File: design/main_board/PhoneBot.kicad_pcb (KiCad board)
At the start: 2 copper layers, 41.3 x 103 mm, 88 parts, among them J101 CX70M-24P1, J102 AVR-ISP-6, J103 Conn_02x03_Odd_Even, J104 Conn_02x03_Odd_Even, J105 Conn_02x03_Odd_Even, J106 Conn_02x03_Odd_Even, SW301 SW_SPDT, U101 ATmega32U4-AU, U201 RN4871, U301 AP2138N-3.3TRG1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

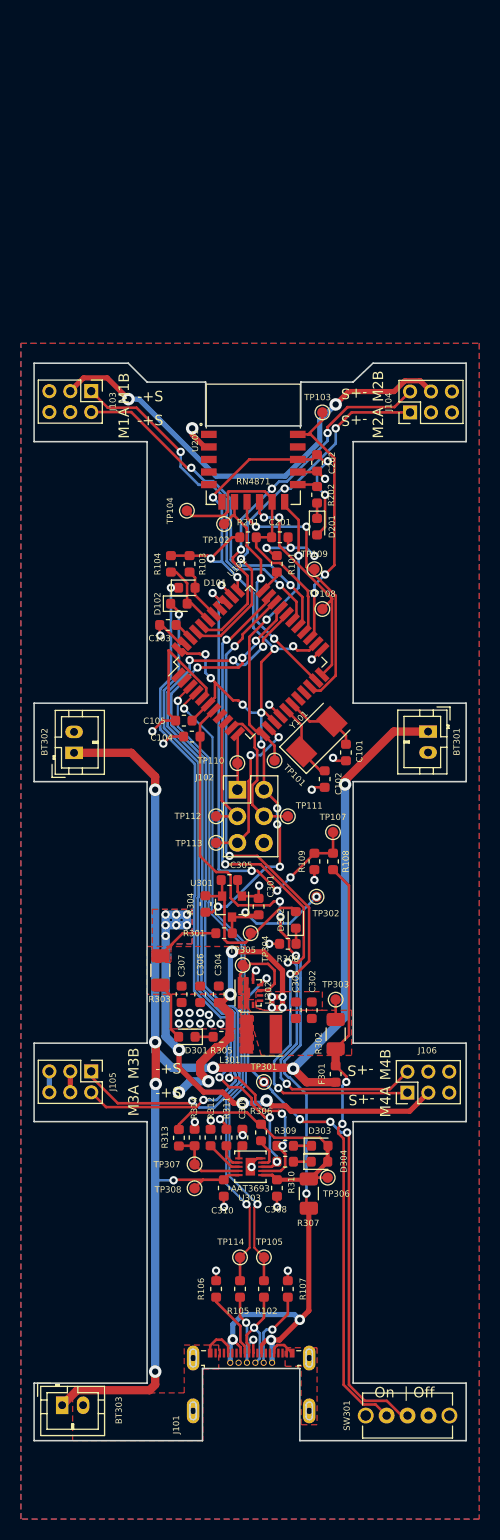
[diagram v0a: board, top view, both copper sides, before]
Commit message: Created esp32 footprint and symbol
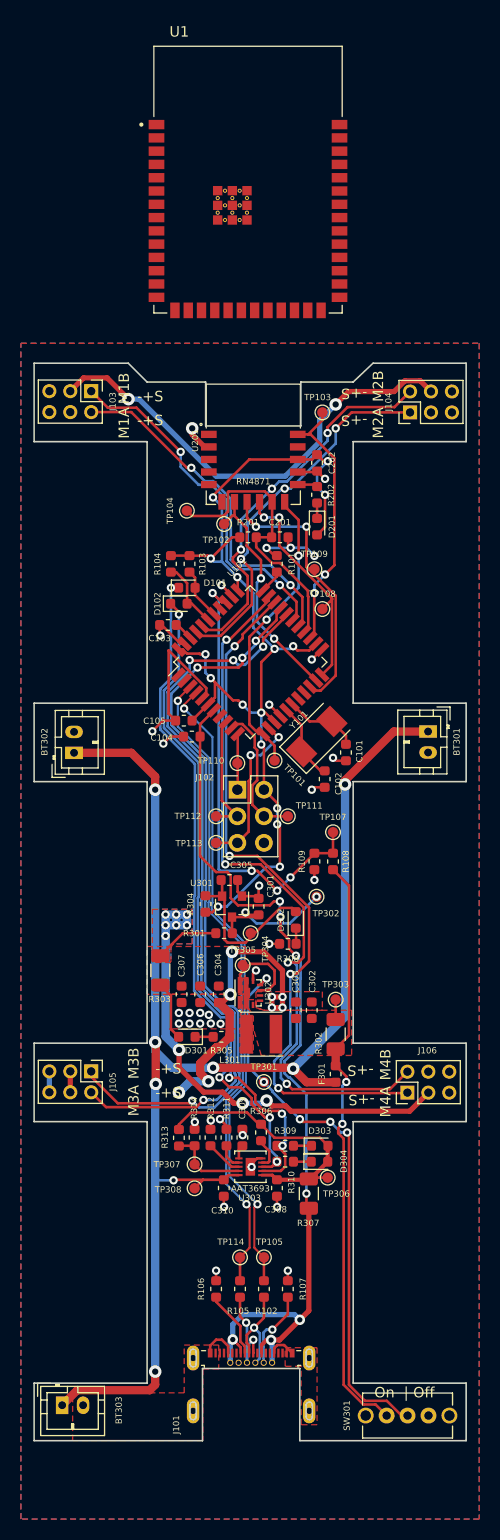
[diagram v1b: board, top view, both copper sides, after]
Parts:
- added U1: ESP32-S3-WROOM-1-N16R8, CustomFootprints:XCVR_ESP32-S3-WROOM-1-N16R8, F.Cu at (-0.25, -53.8)
- R108: value 1k -> 1M
- R109: value 3.6k -> 3.6M
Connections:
- net /VBAT_SENSE renamed /PowerSheet/Vbat
- net /~BLE_RST renamed /~{BLE_RST}
- net /~RST renamed /~{RST}
- J101 pad A10: (no net) -> unconnected-(J101-PadA10)
- J101 pad A11: (no net) -> unconnected-(J101-PadA11)
- J101 pad A2: (no net) -> unconnected-(J101-PadA2)
- J101 pad A3: (no net) -> unconnected-(J101-PadA3)
- J101 pad A8: (no net) -> unconnected-(J101-PadA8)
- J101 pad B10: (no net) -> unconnected-(J101-PadB10)
- J101 pad B11: (no net) -> unconnected-(J101-PadB11)
- J101 pad B2: (no net) -> unconnected-(J101-PadB2)
- J101 pad B3: (no net) -> unconnected-(J101-PadB3)
- J101 pad B8: (no net) -> unconnected-(J101-PadB8)
- U101 pad 1: (no net) -> unconnected-(U101-Pad1)
- U101 pad 18: (no net) -> /SCL
- U101 pad 19: (no net) -> /SDA
- U101 pad 2: (no net) -> unconnected-(U101-Pad2)
- U101 pad 37: (no net) -> unconnected-(U101-Pad37)
- U101 pad 8: (no net) -> unconnected-(U101-Pad8)
- U201 pad 1: (no net) -> unconnected-(U201-Pad1)
- U201 pad 15: (no net) -> unconnected-(U201-Pad15)
- U201 pad 3: (no net) -> unconnected-(U201-Pad3)
- U201 pad 4: (no net) -> unconnected-(U201-Pad4)
- U201 pad 5: (no net) -> unconnected-(U201-Pad5)
- U201 pad 6: (no net) -> unconnected-(U201-Pad6)
